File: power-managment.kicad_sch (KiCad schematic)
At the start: 11 parts, among them J4 ARM, J5 BATTERY, U4 MPM3610GQV-P

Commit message: Reannotated
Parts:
- renumbered R12 to R10, R13 to R11, R14 to R12, R15 to R13, R16 to R14
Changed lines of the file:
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@@
 		(on_board yes)
 		(dnp no)
-		(property "Reference" "#PWR014"
+		(property "Reference" "#PWR050"
 			(at 40.64 29.21 0)
 			(effects
@@
 			(project "Blaze-NT"
 				(path "/2c2eadf0-5503-4531-8753-1a232087fe8c/ff86f43e-2806-4661-a460-b8d13650ca02"
-					(reference "#PWR014")
+					(reference "#PWR050")
 					(unit 1)
 				)
@@
 		(dnp no)
 		(fields_autoplaced yes)
-		(property "Reference" "#PWR061"
+		(property "Reference" "#PWR059"
 			(at 142.24 85.09 0)
 			(effects
@@
 			(project "Blaze-NT"
 				(path "/2c2eadf0-5503-4531-8753-1a232087fe8c/ff86f43e-2806-4661-a460-b8d13650ca02"
-					(reference "#PWR061")
+					(reference "#PWR059")
 					(unit 1)
 				)
@@
 		(dnp no)
 		(fields_autoplaced yes)
-		(property "Reference" "#PWR054"
+		(property "Reference" "#PWR052"
 			(at 45.72 39.37 0)
 			(effects
@@
 			(project "Blaze-NT"
 				(path "/2c2eadf0-5503-4531-8753-1a232087fe8c/ff86f43e-2806-4661-a460-b8d13650ca02"
-					(reference "#PWR054")
+					(reference "#PWR052")
 					(unit 1)
 				)
@@
 		(on_board yes)
 		(dnp no)
-		(property "Reference" "#PWR058"
+		(property "Reference" "#PWR056"
 			(at 55.88 67.31 0)
 			(effects
@@
 			(project "Blaze-NT"
 				(path "/2c2eadf0-5503-4531-8753-1a232087fe8c/ff86f43e-2806-4661-a460-b8d13650ca02"
-					(reference "#PWR058")
+					(reference "#PWR056")
 					(unit 1)
 				)
@@
 		(on_board yes)
 		(dnp no)
-		(property "Reference" "R15"
+		(property "Reference" "R13"
 			(at 59.69 55.88 90)
 			(effects
@@
 			(project "Blaze-NT"
 				(path "/2c2eadf0-5503-4531-8753-1a232087fe8c/ff86f43e-2806-4661-a460-b8d13650ca02"
-					(reference "R15")
+					(reference "R13")
 					(unit 1)
 				)
@@
 		(dnp no)
 		(fields_autoplaced yes)
-		(property "Reference" "#PWR059"
+		(property "Reference" "#PWR057"
 			(at 132.08 67.31 0)
 			(effects
@@
 			(project "Blaze-NT"
 				(path "/2c2eadf0-5503-4531-8753-1a232087fe8c/ff86f43e-2806-4661-a460-b8d13650ca02"
-					(reference "#PWR059")
+					(reference "#PWR057")
 					(unit 1)
 				)
@@
 		(on_board yes)
 		(dnp no)
-		(property "Reference" "R13"
+		(property "Reference" "R11"
 			(at 135.128 55.88 90)
 			(effects
@@
 			(project "Blaze-NT"
 				(path "/2c2eadf0-5503-4531-8753-1a232087fe8c/ff86f43e-2806-4661-a460-b8d13650ca02"
-					(reference "R13")
+					(reference "R11")
 					(unit 1)
 				)
@@
 		(on_board yes)
 		(dnp no)
-		(property "Reference" "#PWR060"
+		(property "Reference" "#PWR058"
 			(at 88.9 80.01 0)
 			(effects
@@
 			(project "Blaze-NT"
 				(path "/2c2eadf0-5503-4531-8753-1a232087fe8c/ff86f43e-2806-4661-a460-b8d13650ca02"
-					(reference "#PWR060")
+					(reference "#PWR058")
 					(unit 1)
 				)
@@
 		(dnp no)
 		(fields_autoplaced yes)
-		(property "Reference" "#PWR062"
+		(property "Reference" "#PWR061"
 			(at 83.82 106.68 0)
 			(effects
@@
 			(project "Blaze-NT"
 				(path "/2c2eadf0-5503-4531-8753-1a232087fe8c/ff86f43e-2806-4661-a460-b8d13650ca02"
-					(reference "#PWR062")
+					(reference "#PWR061")
 					(unit 1)
 				)
@@
 		(on_board yes)
 		(dnp no)
-		(property "Reference" "R12"
+		(property "Reference" "R10"
 			(at 87.376 51.054 90)
 			(effects
@@
 			(project "Blaze-NT"
 				(path "/2c2eadf0-5503-4531-8753-1a232087fe8c/ff86f43e-2806-4661-a460-b8d13650ca02"
-					(reference "R12")
+					(reference "R10")
 					(unit 1)
 				)
@@
 		(on_board yes)
 		(dnp no)
-		(property "Reference" "#PWR057"
+		(property "Reference" "#PWR055"
 			(at 38.1 67.31 0)
 			(effects
@@
 			(project "Blaze-NT"
 				(path "/2c2eadf0-5503-4531-8753-1a232087fe8c/ff86f43e-2806-4661-a460-b8d13650ca02"
-					(reference "#PWR057")
+					(reference "#PWR055")
 					(unit 1)
 				)
@@
 		(on_board yes)
 		(dnp no)
-		(property "Reference" "#PWR056"
+		(property "Reference" "#PWR054"
 			(at 149.86 62.23 0)
 			(effects
@@
 			(project "Blaze-NT"
 				(path "/2c2eadf0-5503-4531-8753-1a232087fe8c/ff86f43e-2806-4661-a460-b8d13650ca02"
-					(reference "#PWR056")
+					(reference "#PWR054")
 					(unit 1)
 				)
@@
 		(on_board yes)
 		(dnp no)
-		(property "Reference" "#PWR053"
+		(property "Reference" "#PWR051"
 			(at 45.72 29.21 0)
 			(effects
@@
 			(project "Blaze-NT"
 				(path "/2c2eadf0-5503-4531-8753-1a232087fe8c/ff86f43e-2806-4661-a460-b8d13650ca02"
-					(reference "#PWR053")
+					(reference "#PWR051")
 					(unit 1)
 				)
@@
 		(on_board yes)
 		(dnp no)
-		(property "Reference" "R14"
+		(property "Reference" "R12"
 			(at 144.272 53.594 90)
 			(effects
@@
 			(project "Blaze-NT"
 				(path "/2c2eadf0-5503-4531-8753-1a232087fe8c/ff86f43e-2806-4661-a460-b8d13650ca02"
-					(reference "R14")
+					(reference "R12")
 					(unit 1)
 				)
@@
 		(on_board yes)
 		(dnp no)
-		(property "Reference" "#PWR055"
+		(property "Reference" "#PWR053"
 			(at 85.09 62.23 0)
 			(effects
@@
 			(project "Blaze-NT"
 				(path "/2c2eadf0-5503-4531-8753-1a232087fe8c/ff86f43e-2806-4661-a460-b8d13650ca02"
-					(reference "#PWR055")
+					(reference "#PWR053")
 					(unit 1)
 				)
@@
 		(on_board yes)
 		(dnp no)
-		(property "Reference" "R16"
+		(property "Reference" "R14"
 			(at 67.31 55.88 90)
 			(effects
@@
 			(project "Blaze-NT"
 				(path "/2c2eadf0-5503-4531-8753-1a232087fe8c/ff86f43e-2806-4661-a460-b8d13650ca02"
-					(reference "R16")
+					(reference "R14")
 					(unit 1)
 				)
@@
 		(on_board yes)
 		(dnp no)
-		(property "Reference" "#PWR037"
+		(property "Reference" "#PWR060"
 			(at 45.72 93.98 0)
 			(effects
@@
 			(project "Blaze-NT"
 				(path "/2c2eadf0-5503-4531-8753-1a232087fe8c/ff86f43e-2806-4661-a460-b8d13650ca02"
-					(reference "#PWR037")
+					(reference "#PWR060")
 					(unit 1)
 				)
@@
 		(dnp no)
 		(fields_autoplaced yes)
-		(property "Reference" "#FLG04"
+		(property "Reference" "#FLG02"
 			(at 38.1 59.055 0)
 			(effects
@@
 			(project ""
 				(path "/2c2eadf0-5503-4531-8753-1a232087fe8c/ff86f43e-2806-4661-a460-b8d13650ca02"
-					(reference "#FLG04")
-					(unit 1)
-				)
+					(reference "#FLG02")
+					(unit 1)
+				)

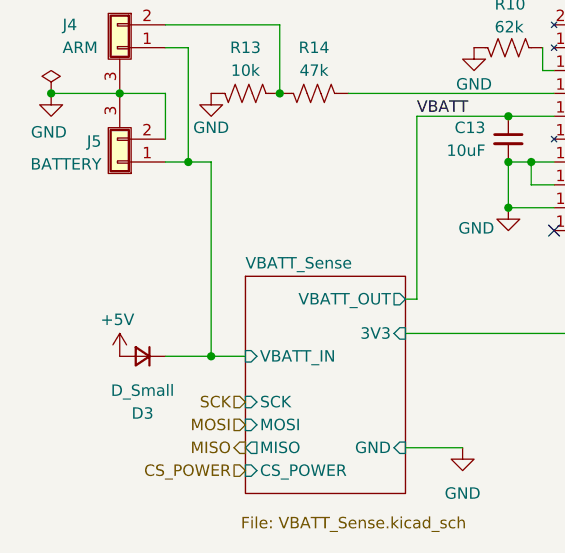
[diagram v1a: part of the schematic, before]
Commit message: Footprint selection
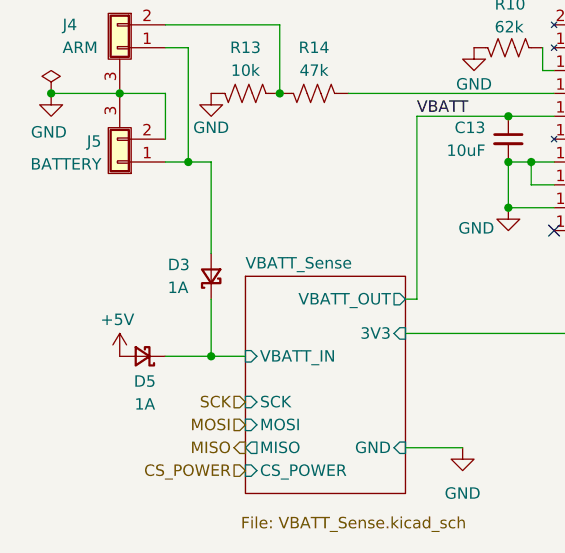
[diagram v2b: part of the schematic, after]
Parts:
- removed D3: D_Small, symbol Device:D_Small
- added D3, D5: 1A, Diode_SMD:D_SOD-123F, symbol Device:D_Schottky_Small
- C13, C14: footprint (none) -> Capacitor_SMD:C_0603_1608Metric
- R10, R11, R12, R13, R14: footprint (none) -> Resistor_SMD:R_0603_1608Metric
- U4: footprint (none) -> Avionics_Feet:MPM3610QGV-P
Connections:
- net +5V: now also D5.2 (A)
- net VBATT_Sense/VBATT_IN: now also D3.1 (K), D5.1 (K); no longer J4.1 (Pin_2), J5.1 (Pin_1)
- new net: D3.2 (A), J4.1 (Pin_2), J5.1 (Pin_1)
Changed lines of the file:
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@@
+	)
+	(junction
+		(at 132.08 58.42)
+		(diameter 0)
+		(color 0 0 0 0)
+	)
+	(junction
+		(at 45.72 60.96)
+		(diameter 0)
+		(color 0 0 0 0)
 	)
 	(junction
@@
 	)
 	(junction
-		(at 132.08 58.42)
-		(diameter 0)
-		(color 0 0 0 0)
-	)
-	(junction
-		(at 45.72 60.96)
-		(diameter 0)
-		(color 0 0 0 0)
-	)
-	(junction
 		(at 142.24 58.42)
 		(diameter 0)
@@
 	(wire
 		(pts
+			(xy 55.88 90.17) (xy 59.69 90.17)
+		)
+		(stroke
+			(width 0)
+			(type default)
+		)
+	)
+	(wire
+		(pts
+			(xy 55.88 83.82) (xy 55.88 90.17)
+		)
+		(stroke
+			(width 0)
+			(type default)
+		)
+	)
+	(wire
+		(pts
 			(xy 125.73 66.04) (xy 125.73 63.5)
 		)
@@
 	(wire
 		(pts
-			(xy 55.88 68.58) (xy 55.88 90.17)
-		)
-		(stroke
-			(width 0)
-			(type default)
-		)
-	)
-	(wire
-		(pts
 			(xy 88.9 63.5) (xy 93.98 63.5)
 		)
@@
 	(wire
 		(pts
-			(xy 55.88 90.17) (xy 59.69 90.17)
+			(xy 50.8 90.17) (xy 55.88 90.17)
 		)
 		(stroke
@@
 	(wire
 		(pts
-			(xy 50.8 90.17) (xy 55.88 90.17)
-		)
-		(stroke
-			(width 0)
-			(type default)
-		)
-	)
-	(wire
-		(pts
 			(xy 127 71.12) (xy 142.24 71.12)
 		)
@@
 		(pts
 			(xy 78.74 63.5) (xy 88.9 63.5)
+		)
+		(stroke
+			(width 0)
+			(type default)
+		)
+	)
+	(wire
+		(pts
+			(xy 55.88 68.58) (xy 55.88 78.74)
 		)
 		(stroke
@@
 	)
 	(symbol
-		(lib_id "Device:D_Small")
-		(at 48.26 90.17 180)
-		(unit 1)
-		(exclude_from_sim no)
-		(in_bom yes)
-		(on_board yes)
-		(dnp no)
-		(property "Reference" "D3"
-			(at 48.26 96.52 0)
-			(effects
-				(font
-					(size 1.27 1.27)
-				)
-			)
-		)
-		(property "Value" "D_Small"
-			(at 48.26 93.98 0)
-			(effects
-				(font
-					(size 1.27 1.27)
-				)
-			)
-		)
-		(property "Footprint" ""
-			(at 48.26 90.17 90)
-			(effects
-				(font
-					(size 1.27 1.27)
-				)
-				(hide yes)
-			)
-		)
-		(property "Datasheet" "~"
-			(at 48.26 90.17 90)
-			(effects
-				(font
-					(size 1.27 1.27)
-				)
-				(hide yes)
-			)
-		)
-		(property "Description" "Diode, small symbol"
-			(at 48.26 90.17 0)
-			(effects
-				(font
-					(size 1.27 1.27)
-				)
-				(hide yes)
-			)
-		)
-		(property "Sim.Device" "D"
-			(at 48.26 90.17 0)
-			(effects
-				(font
-					(size 1.27 1.27)
-				)
-				(hide yes)
-			)
-		)
-		(property "Sim.Pins" "1=K 2=A"
-			(at 48.26 90.17 0)
-			(effects
-				(font
-					(size 1.27 1.27)
-				)
-				(hide yes)
-			)
-		)
-		(pin "1"
-		)
-		(pin "2"
-		)
-		(instances
-			(project ""
-				(path "/2c2eadf0-5503-4531-8753-1a232087fe8c/ff86f43e-2806-4661-a460-b8d13650ca02"
-					(reference "D3")
-					(unit 1)
-				)
-			)
-		)
-	)
-	(symbol
 		(lib_id "power:GND")
 		(at 55.88 60.96 0)
@@
 			)
 		)
-		(property "Footprint" ""
+		(property "Footprint" "Resistor_SMD:R_0603_1608Metric"
 			(at 59.436 59.944 90)
 			(effects
@@
 				(path "/4a897c16-693b-45fb-822c-5a4e67f889c4"
 					(reference "R3")
+					(unit 1)
+				)
+			)
+		)
+	)
+	(symbol
+		(lib_id "Device:D_Schottky_Small")
+		(at 48.26 90.17 180)
+		(unit 1)
+		(exclude_from_sim no)
+		(in_bom yes)
+		(on_board yes)
+		(dnp no)
+		(property "Reference" "D5"
+			(at 48.514 92.964 0)
+			(effects
+				(font
+					(size 1.27 1.27)
+				)
+			)
+		)
+		(property "Value" "1A"
+			(at 48.514 95.504 0)
+			(effects
+				(font
+					(size 1.27 1.27)
+				)
+			)
+		)
+		(property "Footprint" "Diode_SMD:D_SOD-123F"
+			(at 48.26 90.17 90)
+			(effects
+				(font
+					(size 1.27 1.27)
+				)
+				(hide yes)
+			)
+		)
+		(property "Datasheet" "~"
+			(at 48.26 90.17 90)
+			(effects
+				(font
+					(size 1.27 1.27)
+				)
+				(hide yes)
+			)
+		)
+		(property "Description" "Schottky diode, small symbol"
+			(at 48.26 90.17 0)
+			(effects
+				(font
+					(size 1.27 1.27)
+				)
+				(hide yes)
+			)
+		)
+		(pin "2"
+		)
+		(pin "1"
+		)
+		(instances
+			(project ""
+				(path "/2c2eadf0-5503-4531-8753-1a232087fe8c/ff86f43e-2806-4661-a460-b8d13650ca02"
+					(reference "D5")
 					(unit 1)
 				)
@@
 			)
 		)
-		(property "Footprint" ""
+		(property "Footprint" "Capacitor_SMD:C_0603_1608Metric"
 			(at 141.2748 78.74 0)
 			(effects
@@
 			)
 		)
-		(property "Footprint" ""
+		(property "Footprint" "Resistor_SMD:R_0603_1608Metric"
 			(at 135.636 57.404 90)
 			(effects
@@
 			)
 		)
-		(property "Footprint" ""
+		(property "Footprint" "Resistor_SMD:R_0603_1608Metric"
 			(at 89.154 56.896 90)
 			(effects
@@
 			)
 		)
-		(property "Footprint" ""
+		(property "Footprint" "Avionics_Feet:MPM3610QGV-P"
 			(at 113.792 36.576 0)
 			(effects
@@
 				(path "/2c2eadf0-5503-4531-8753-1a232087fe8c/ff86f43e-2806-4661-a460-b8d13650ca02"
 					(reference "U4")
+					(unit 1)
+				)
+			)
+		)
+	)
+	(symbol
+		(lib_id "Device:D_Schottky_Small")
+		(at 55.88 81.28 90)
+		(unit 1)
+		(exclude_from_sim no)
+		(in_bom yes)
+		(on_board yes)
+		(dnp no)
+		(property "Reference" "D3"
+			(at 51.054 80.01 90)
+			(effects
+				(font
+					(size 1.27 1.27)
+				)
+				(justify right)
+			)
+		)
+		(property "Value" "1A"
+			(at 51.054 82.55 90)
+			(effects
+				(font
+					(size 1.27 1.27)
+				)
+				(justify right)
+			)
+		)
+		(property "Footprint" "Diode_SMD:D_SOD-123F"
+			(at 55.88 81.28 90)
+			(effects
+				(font
+					(size 1.27 1.27)
+				)
+				(hide yes)
+			)
+		)
+		(property "Datasheet" "~"
+			(at 55.88 81.28 90)
+			(effects
+				(font
+					(size 1.27 1.27)
+				)
+				(hide yes)
+			)
+		)
+		(property "Description" "Schottky diode, small symbol"
+			(at 55.88 81.28 0)
+			(effects
+				(font
+					(size 1.27 1.27)
+				)
+				(hide yes)
+			)
+		)
+		(pin "2"
+		)
+		(pin "1"
+		)
+		(instances
+			(project "Blaze-NT"
+				(path "/2c2eadf0-5503-4531-8753-1a232087fe8c/ff86f43e-2806-4661-a460-b8d13650ca02"
+					(reference "D3")
 					(unit 1)
 				)
@@
 			)
 		)
-		(property "Footprint" ""
+		(property "Footprint" "Capacitor_SMD:C_0603_1608Metric"
 			(at 88.9 66.04 0)
 			(effects
@@
 			)
 		)
-		(property "Footprint" ""
+		(property "Footprint" "Resistor_SMD:R_0603_1608Metric"
 			(at 145.796 57.404 90)
 			(effects
@@
 			)
 		)
-		(property "Footprint" ""
+		(property "Footprint" "Resistor_SMD:R_0603_1608Metric"
 			(at 67.056 59.944 90)
 			(effects

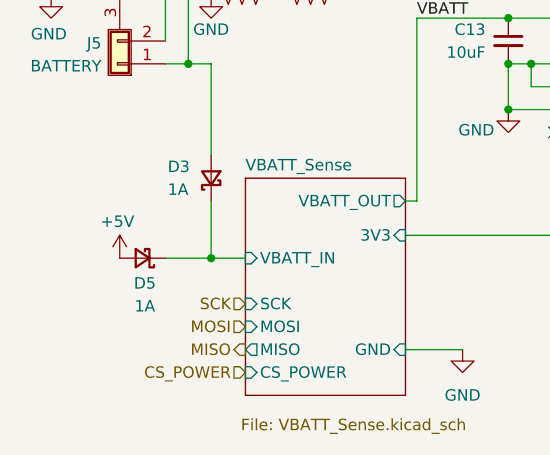
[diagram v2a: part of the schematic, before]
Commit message: Radio footprint selection
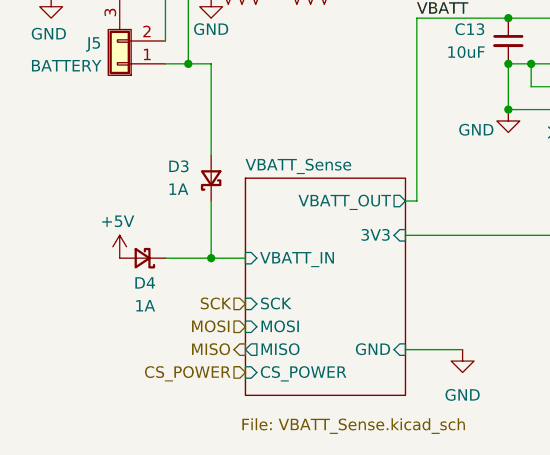
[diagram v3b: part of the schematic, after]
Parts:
- renumbered D5 to D4
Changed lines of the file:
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@@
 		(on_board yes)
 		(dnp no)
-		(property "Reference" "D5"
+		(property "Reference" "D4"
 			(at 48.514 92.964 0)
 			(effects
@@
 			(project ""
 				(path "/2c2eadf0-5503-4531-8753-1a232087fe8c/ff86f43e-2806-4661-a460-b8d13650ca02"
-					(reference "D5")
+					(reference "D4")
 					(unit 1)
 				)

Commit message: Addeed part numbers
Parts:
- added D5: LED, LED_SMD:LED_0603_1608Metric, symbol Device:LED
- added R18: 120, Resistor_SMD:R_0603_1608Metric, symbol Device:R_US
- C13: LCSC (none) -> C96446
- C14: LCSC (none) -> C59461
- D3, D4: LCSC (none) -> C784540
- R10: LCSC (none) -> C137694
- R11: LCSC (none) -> C137760
- R12: LCSC (none) -> C114636
- R13: LCSC (none) -> C98220
- R14: LCSC (none) -> C105579
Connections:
- net +3V3: now also D5.2 (A)
- net GND: now also R18.1
- new net: D5.1 (K), R18.2

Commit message: Added Digikey Components
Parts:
- D3, D4: Digikey (none) -> SS24FL
- D5: Digikey (none) -> LTST-C191KRKT
- J4, J5: Digikey (none) -> WM17581-ND
- U4: Digikey (none) -> 1589-1250-1-ND
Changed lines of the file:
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@@
+			)
+		)
+		(property "Digikey" ""
+			(at 59.69 60.96 90)
+			(effects
+				(font
+					(size 1.27 1.27)
+				)
+				(hide yes)
 			)
 		)
@@
 			)
 		)
+		(property "Digikey" "LTST-C191KRKT"
+			(at 153.67 87.63 0)
+			(effects
+				(font
+					(size 1.27 1.27)
+				)
+				(hide yes)
+			)
+		)
 		(pin "2"
 		)
@@
 		)
 		(property "LCSC" "C784540"
+			(at 48.26 90.17 0)
+			(effects
+				(font
+					(size 1.27 1.27)
+				)
+				(hide yes)
+			)
+		)
+		(property "Digikey" "SS24FL"
 			(at 48.26 90.17 0)
 			(effects
@@
 			)
 		)
+		(property "Digikey" ""
+			(at 161.29 87.63 90)
+			(effects
+				(font
+					(size 1.27 1.27)
+				)
+				(hide yes)
+			)
+		)
 		(pin "2"
 		)
@@
 			)
 		)
+		(property "Digikey" ""
+			(at 142.24 74.93 0)
+			(effects
+				(font
+					(size 1.27 1.27)
+				)
+				(hide yes)
+			)
+		)
 		(pin "1"
 		)
@@
 			)
 		)
+		(property "Digikey" ""
+			(at 135.89 58.42 90)
+			(effects
+				(font
+					(size 1.27 1.27)
+				)
+				(hide yes)
+			)
+		)
 		(pin "1"
 		)
@@
 			)
 		)
+		(property "Digikey" ""
+			(at 88.9 55.88 90)
+			(effects
+				(font
+					(size 1.27 1.27)
+				)
+				(hide yes)
+			)
+		)
 		(pin "2"
 		)
@@
 			)
 		)
+		(property "Digikey" "1589-1250-1-ND"
+			(at 88.9 53.34 0)
+			(effects
+				(font
+					(size 1.27 1.27)
+				)
+				(hide yes)
+			)
+		)
 		(pin "18"
 		)
@@
 		)
 		(property "LCSC" "C784540"
+			(at 55.88 81.28 90)
+			(effects
+				(font
+					(size 1.27 1.27)
+				)
+				(hide yes)
+			)
+		)
+		(property "Digikey" "SS24FL"
 			(at 55.88 81.28 90)
 			(effects
@@
 		)
 		(property "LCSC" ""
+			(at 45.72 68.58 0)
+			(effects
+				(font
+					(size 1.27 1.27)
+				)
+				(hide yes)
+			)
+		)
+		(property "Digikey" "WM17581-ND"
 			(at 45.72 68.58 0)
 			(effects
@@
 			)
 		)
+		(property "Digikey" "WM17581-ND"
+			(at 45.72 53.34 0)
+			(effects
+				(font
+					(size 1.27 1.27)
+				)
+				(hide yes)
+			)
+		)
 		(pin "3"
 		)
@@
 			)
 		)
+		(property "Digikey" ""
+			(at 88.9 66.04 0)
+			(effects
+				(font
+					(size 1.27 1.27)
+				)
+				(hide yes)
+			)
+		)
 		(pin "2"
 		)
@@
 			)
 		)
+		(property "Digikey" ""
+			(at 146.05 58.42 90)
+			(effects
+				(font
+					(size 1.27 1.27)
+				)
+				(hide yes)
+			)
+		)
 		(pin "1"
 		)
@@
 			(at 67.31 60.96 90)
 			(effects
+				(font
+					(size 1.27 1.27)
+				)
+				(hide yes)
+			)
+		)
+		(property "Digikey" ""
+			(at 67.31 60.96 90)
+			(effects
